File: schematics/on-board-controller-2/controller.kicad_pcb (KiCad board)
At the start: 2 copper layers, 90 x 60 mm, 75 parts, among them J1 5-1814832-1, J2 programmer, J3 xt60, M1 Motor_DC, M2 Motor_DC, M3 Stepper_Motor_bipolar, Q1 NMOS, U1 L293D, U2 STM32L476RGTx, U3 L293D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

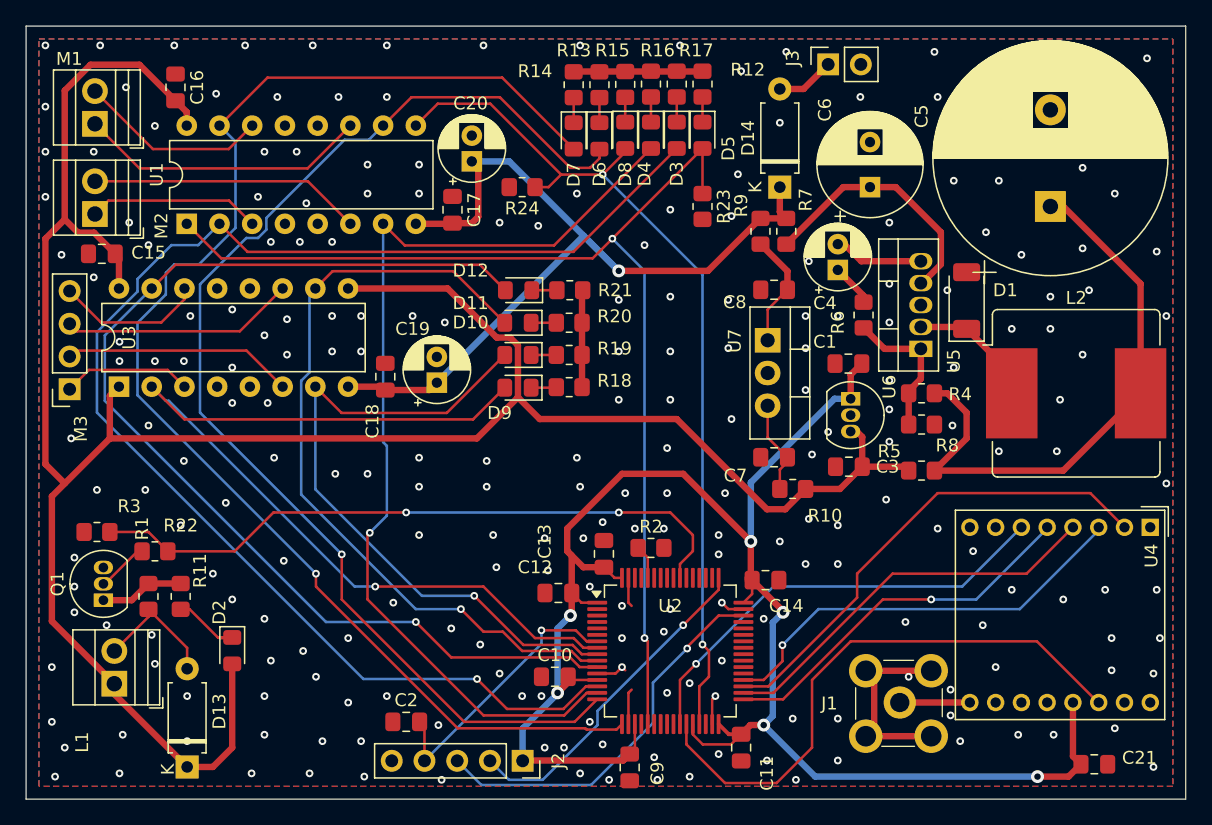
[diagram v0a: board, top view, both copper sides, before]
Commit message: updated footprints for through hole components with long legs
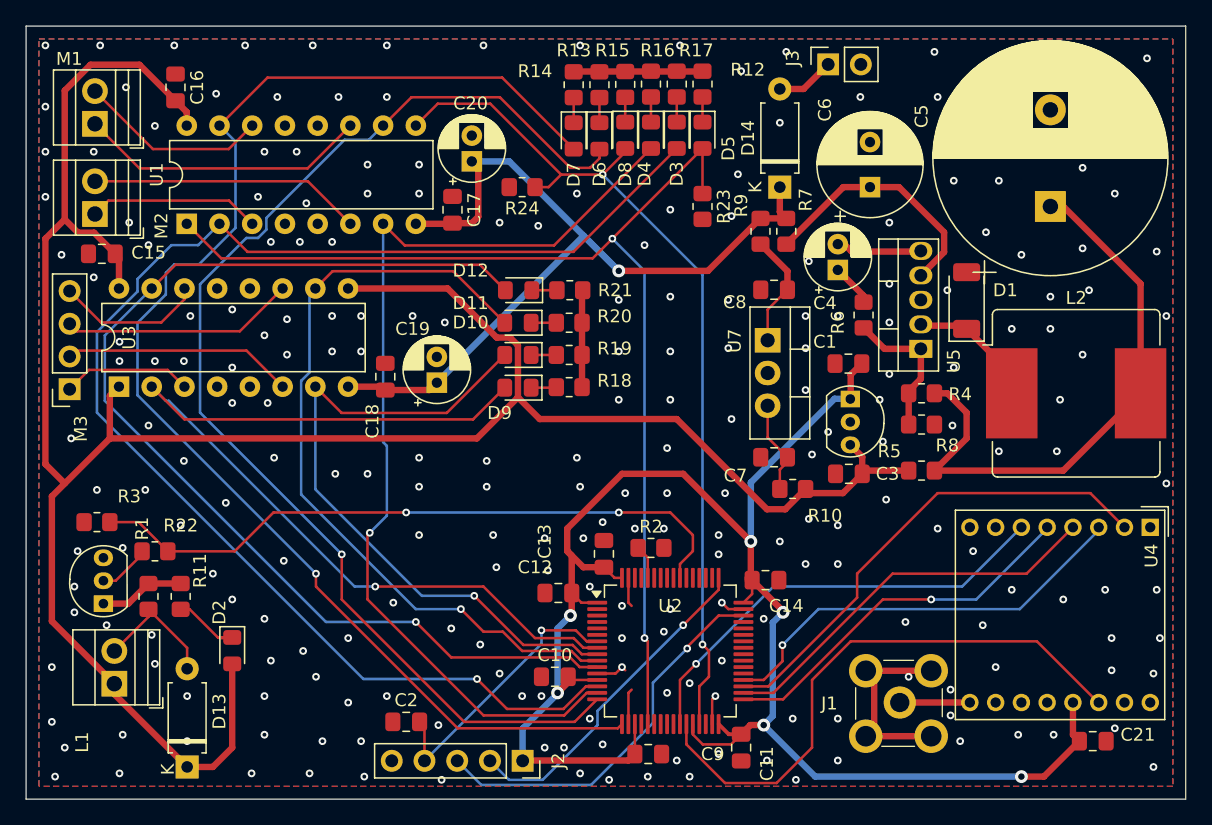
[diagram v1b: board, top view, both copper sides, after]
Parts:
- moved C21 1.80 mm to (145.3, 116.0)
- moved C9 1.77 mm to (110.8, 117.0), turned to 180 degrees
- moved R3 0.77 mm to (68.0, 99.0)
- moved C3 0.55 mm to (126.4, 95.2)
- moved Q1 0.32 mm to (68.2, 105.2)
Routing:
- net +6V: track 190.7 -> 189.6 mm
- net +3V3: track 137.5 -> 136.5 mm
- net GND: vias 245 -> 246
